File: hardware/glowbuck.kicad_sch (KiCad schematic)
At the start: 37 parts, among them J101 Conn_01x01_Pin, J102 Conn_01x01_Pin, J103 Conn_01x01_Pin, J104 Conn_01x01_Pin, J105 Conn_01x01_Pin, J106 Conn_01x01_Pin, J107 Conn_01x01_Pin, J108 Conn_01x01_Pin, J109 Conn_01x01_Pin, J110 Conn_02x08_Counter_Clockwise, SW101 SW_Push, SW102 SW_Push, SW103 SW_Push, U101 ESP32-S3-WROOM-1

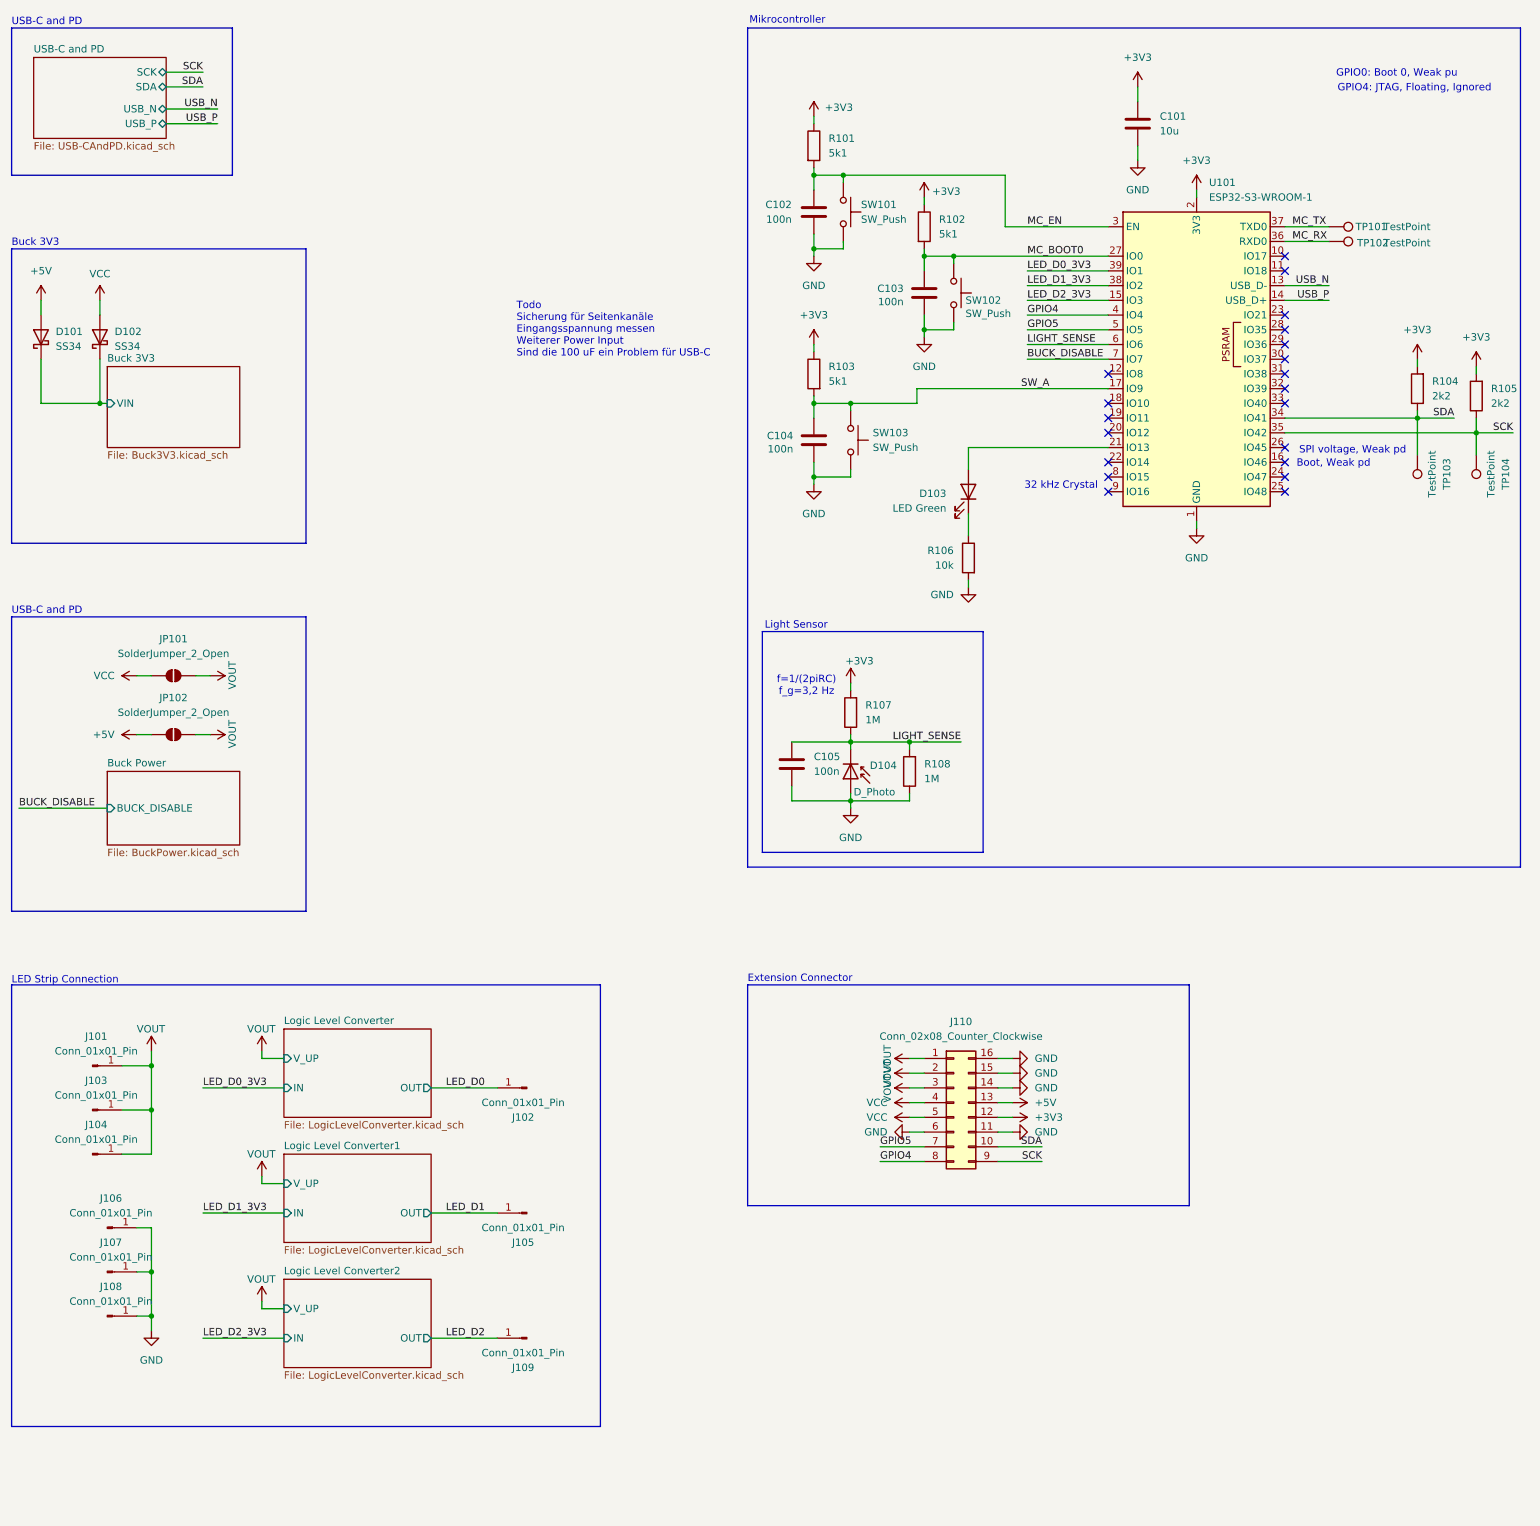
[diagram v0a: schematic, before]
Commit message: Optimized BOM and added netties
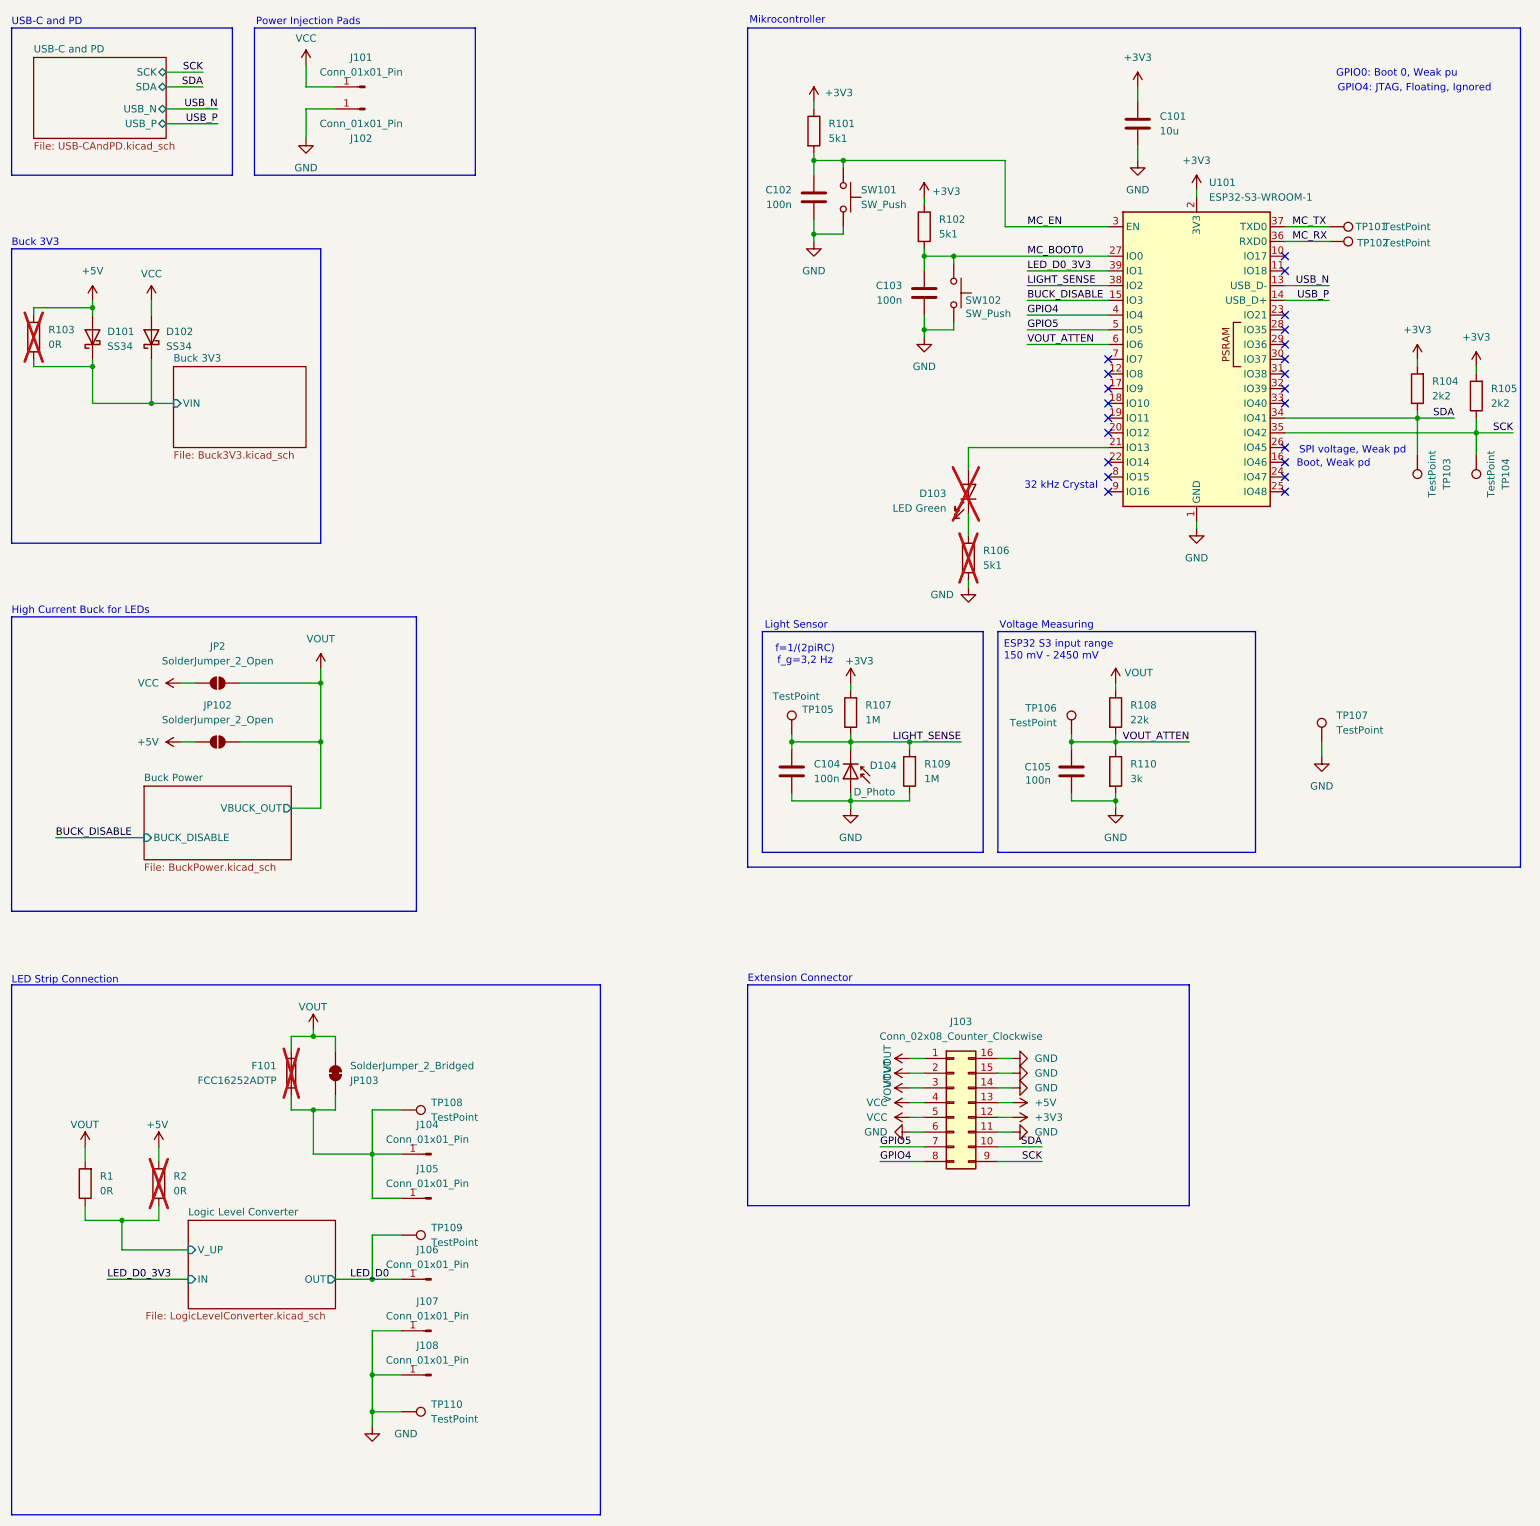
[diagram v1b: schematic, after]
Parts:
- removed C104: 100n, Capacitor_SMD:C_0603_1608Metric_Pad1.08x0.95mm_HandSolder, symbol Device:C
- removed J103, J106, J109: Conn_01x01_Pin, symbol Connector:Conn_01x01_Pin
- removed JP101: SolderJumper_2_Open, Jumper:SolderJumper-2_P1.3mm_Open_Pad1.0x1.5mm, symbol Jumper:SolderJumper_2_Open
- removed SW103: SW_Push, rise:PTS526_GPins_NoGround_2Pole, symbol Switch:SW_Push
- added C105: 100n, Capacitor_SMD:C_0603_1608Metric_Pad1.08x0.95mm_HandSolder, symbol Device:C
- added F101: FCC16252ADTP, Fuse:Fuse_0603_1608Metric, symbol Device:Fuse
- added J102: Conn_01x01_Pin, TestPoint:TestPoint_Pad_3.0x3.0mm, symbol Connector:Conn_01x01_Pin
- added JP103: SolderJumper_2_Bridged, glowbuck:SolderJumper_Open_HighCurrent, symbol Jumper:SolderJumper_2_Bridged
- added JP2: SolderJumper_2_Open, glowbuck:SolderJumper_Open_HighCurrent, symbol Jumper:SolderJumper_2_Open
- added R1, R2: 0R, Resistor_SMD:R_0603_1608Metric_Pad0.98x0.95mm_HandSolder, symbol Device:R
- added R108: 22k, Resistor_SMD:R_0603_1608Metric_Pad0.98x0.95mm_HandSolder, symbol Device:R
- added R110: 3k, Resistor_SMD:R_0603_1608Metric_Pad0.98x0.95mm_HandSolder, symbol Device:R
- added TP105, TP106, TP107, TP108, TP109, TP110: TestPoint, TestPoint:TestPoint_Pad_D1.0mm, symbol Connector:TestPoint
- D103: now not fitted
- J101, J104, J105, J107, J108: footprint (none) -> TestPoint:TestPoint_Pad_3.0x3.0mm
- J106: renamed from J102; footprint (none) -> TestPoint:TestPoint_Pad_2.0x2.0mm
- JP102: footprint Jumper:SolderJumper-2_P1.3mm_Open_Pad1.0x1.5mm -> glowbuck:SolderJumper_Open_HighCurrent
- R103: value 5k1 -> 0R; MouserNumber 652-CRT0603FZ1002ELF -> 603-RC0603FR-130RL; Var (none) -> Debug Included(0R) Excluded(-! DNP); now not fitted
- R106: value 10k -> 5k1; now not fitted; now left out of the parts list
- TP101, TP102, TP103, TP104: footprint TestPoint:TestPoint_Pad_D1.5mm -> TestPoint:TestPoint_Pad_D1.0mm
- renumbered C105 to C104, J110 to J103, R108 to R109
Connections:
- net LED_D1_3V3 is gone; now on net LIGHT_SENSE: U101.38 (IO2)
- net LED_D2_3V3 is gone; now on net BUCK_DISABLE: U101.15 (IO3)
- net +3V3: no longer R103.1
- net +5V: now also R103.2, R2.2
- net BUCK_DISABLE: no longer U101.7 (IO7)
- net Buck 3V3/VIN: now also R103.1
- net GND: now also C105.2, J102.1 (Pin_1), R110.2, TP107.1, TP110.1
- net LED_D0: now also TP109.1
- net LIGHT_SENSE: now also TP105.1; no longer U101.6 (IO6)
- net VCC: now also J101.1 (Pin_1), JP2.1 (A)
- net VOUT: now also F101.2, JP103.2 (B), JP2.2 (B), R1.2, R108.1; no longer J101.1 (Pin_1), J104.1 (Pin_1)
- net LED_D1: no longer names the net of J105.1 (Pin_1)
- net LED_D1: now also J104.1 (Pin_1), F101.1, JP103.1 (A), TP108.1
- net SW_A: no longer names the net of U101.17 (IO9)
- net SW_A: no longer R103.2
- new net Logic Level Converter/V_UP: R1.1, R2.1
- new net VOUT_ATTEN: C105.1, R108.2, R110.1, TP106.1, U101.6 (IO6)
- no-connect marks 20 -> 22
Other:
- removed sheet Logic Level Converter1
- removed sheet Logic Level Converter2
- sheet Buck Power ports: added VBUCK_OUT; removed none
- note added: "ESP32 S3 input range 150 mV - 2450 mV"
- note added: "High Current Buck for LEDs"
- note added: "Power Injection Pads"
- note added: "Voltage Measuring"
- note removed: "Todo Sicherung für Seitenkanäle Eingangsspannung messen Weiterer Power Input Sind die 100 uF ein Problem für USB-C"
- moved on the sheet: C102, C104, D101, D102, J106, JP102, R101, SW101

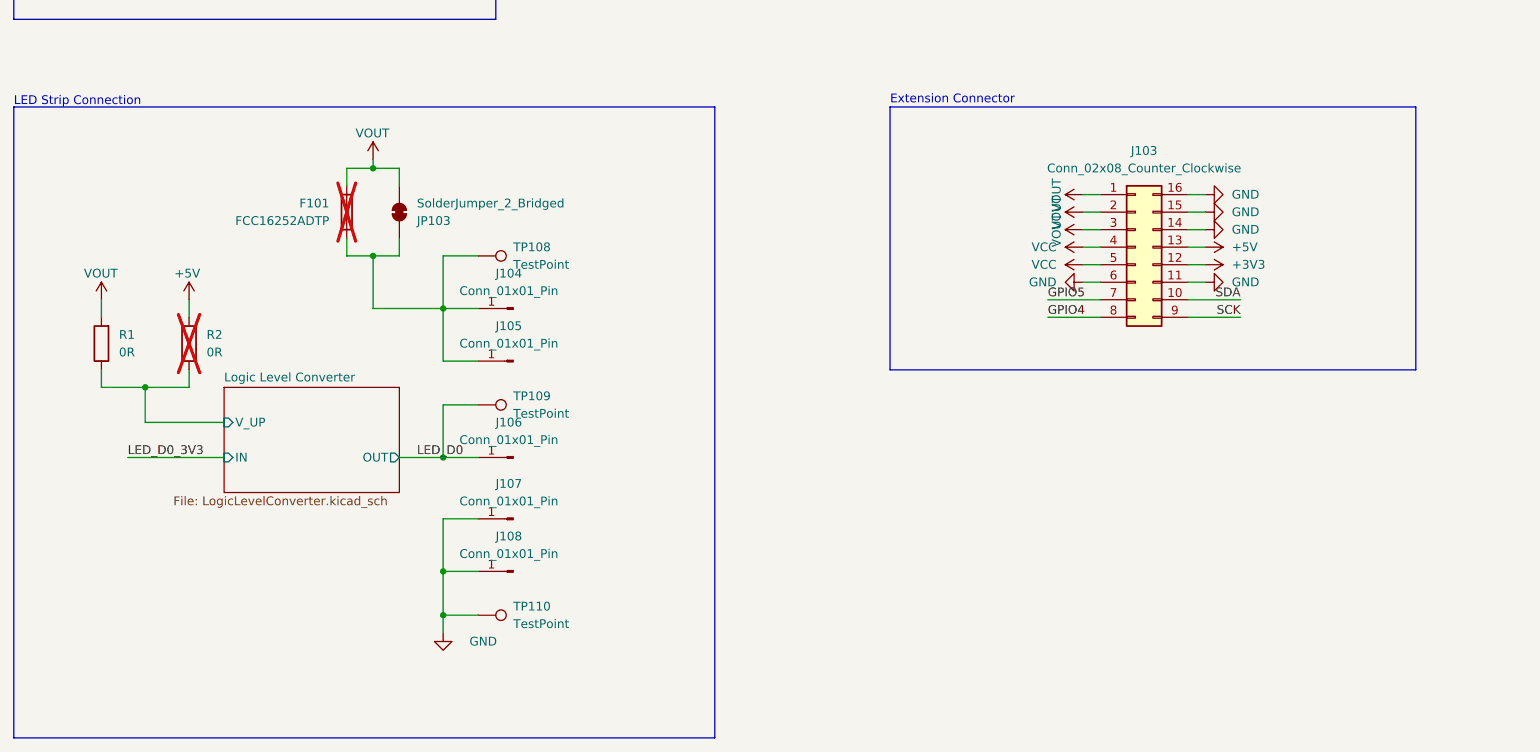
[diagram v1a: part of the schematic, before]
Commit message: Spring terminal, finalising PD settings, checking buck 10 A
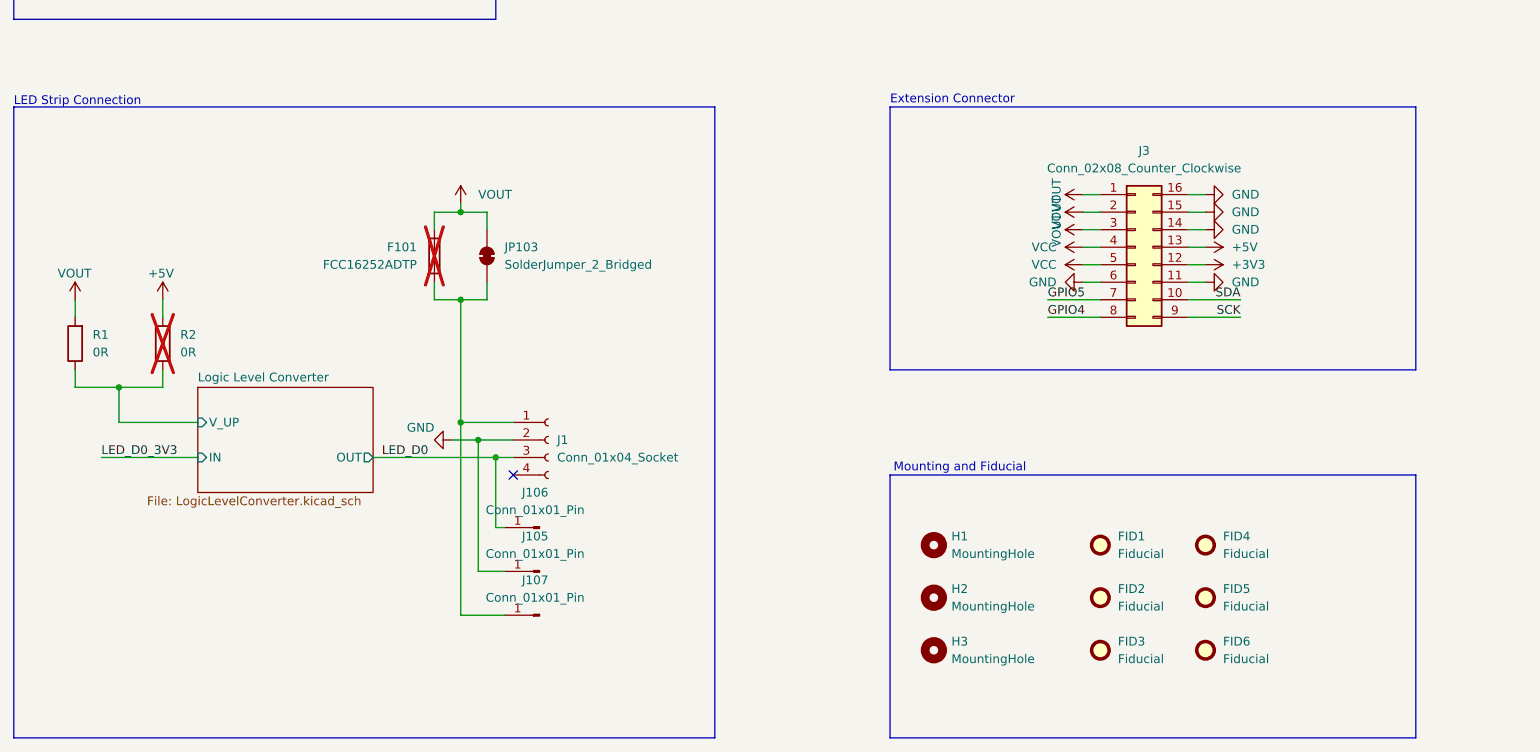
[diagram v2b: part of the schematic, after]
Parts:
- removed J103: Conn_02x08_Counter_Clockwise, Connector_PinHeader_2.54mm:PinHeader_2x08_P2.54mm_Vertical_SMD, symbol Connector_Generic:Conn_02x08_Counter_Clockwise
- removed J104, J108: Conn_01x01_Pin, TestPoint:TestPoint_Pad_3.0x3.0mm, symbol Connector:Conn_01x01_Pin
- removed TP108, TP109, TP110: TestPoint, TestPoint:TestPoint_Pad_D1.0mm, symbol Connector:TestPoint
- added FID1, FID2, FID3, FID4, FID5, FID6: Fiducial, Fiducial:Fiducial_0.5mm_Mask1mm, symbol Mechanical:Fiducial
- added H1, H2, H3: MountingHole, MountingHole:MountingHole_2.2mm_M2_DIN965_Pad_TopBottom, symbol Mechanical:MountingHole
- added J1: Conn_01x04_Socket, glowbuck:PTS 1,5_ 4-5,0-H, symbol Connector:Conn_01x04_Socket
- added J3: Conn_02x08_Counter_Clockwise, Connector_PinHeader_2.54mm:PinHeader_2x08_P2.54mm_Vertical, symbol Connector_Generic:Conn_02x08_Counter_Clockwise
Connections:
- net +3V3: now also J3.12 (Pin_12)
- net +5V: now also J3.13 (Pin_13)
- net GND: now also J105.1 (Pin_1), J1.2 (Pin_2), J3.11 (Pin_11), J3.14 (Pin_14), J3.15 (Pin_15), J3.16 (Pin_16), J3.6 (Pin_6); no longer J107.1 (Pin_1)
- net GPIO4: now also J3.8 (Pin_8)
- net GPIO5: now also J3.7 (Pin_7)
- net LED_D0: now also J1.3 (Pin_3)
- net SCK: now also J3.9 (Pin_9)
- net SDA: now also J3.10 (Pin_10)
- net VCC: now also J3.4 (Pin_4), J3.5 (Pin_5)
- net VOUT: now also J3.1 (Pin_1), J3.2 (Pin_2), J3.3 (Pin_3)
- net at F101.1, JP103.1 (A): now also J107.1 (Pin_1), J1.1 (Pin_1); no longer J105.1 (Pin_1)
- no-connect marks 22 -> 23
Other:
- note added: "Mounting and Fiducial"
- moved on the sheet: F101, J105, J106, J107, JP103, R1, R2
